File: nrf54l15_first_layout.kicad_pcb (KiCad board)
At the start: 4 copper layers, 76.4 x 51 mm, 60 parts, among them CN1 SM04B-SRSS-TB, J2 TC2030, J3 USB_C_Receptacle_PowerOnly_6P, U1 nRF54L15-QDXX, U2 nPM1300-QEXX, U3 SPV1040T, U4 S2B-PH-K-S-GW, X1 XL7EL89CKI-111YLC-32M

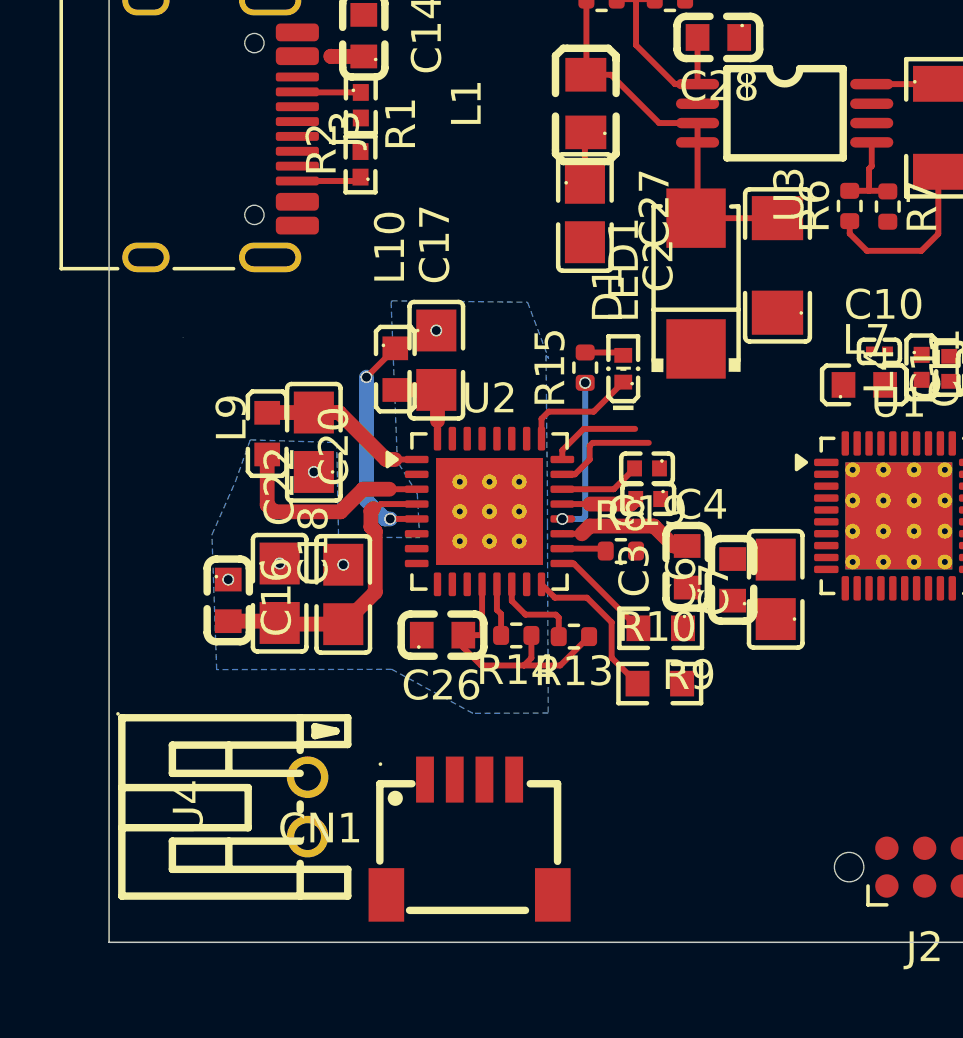
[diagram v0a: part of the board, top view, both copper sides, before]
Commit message: Update soil moisture PCB and npm1300 VDDIO routing; add espc6_ph and first layout projects.
Co-authored-by: Cursor <cursoragent@cursor.com>
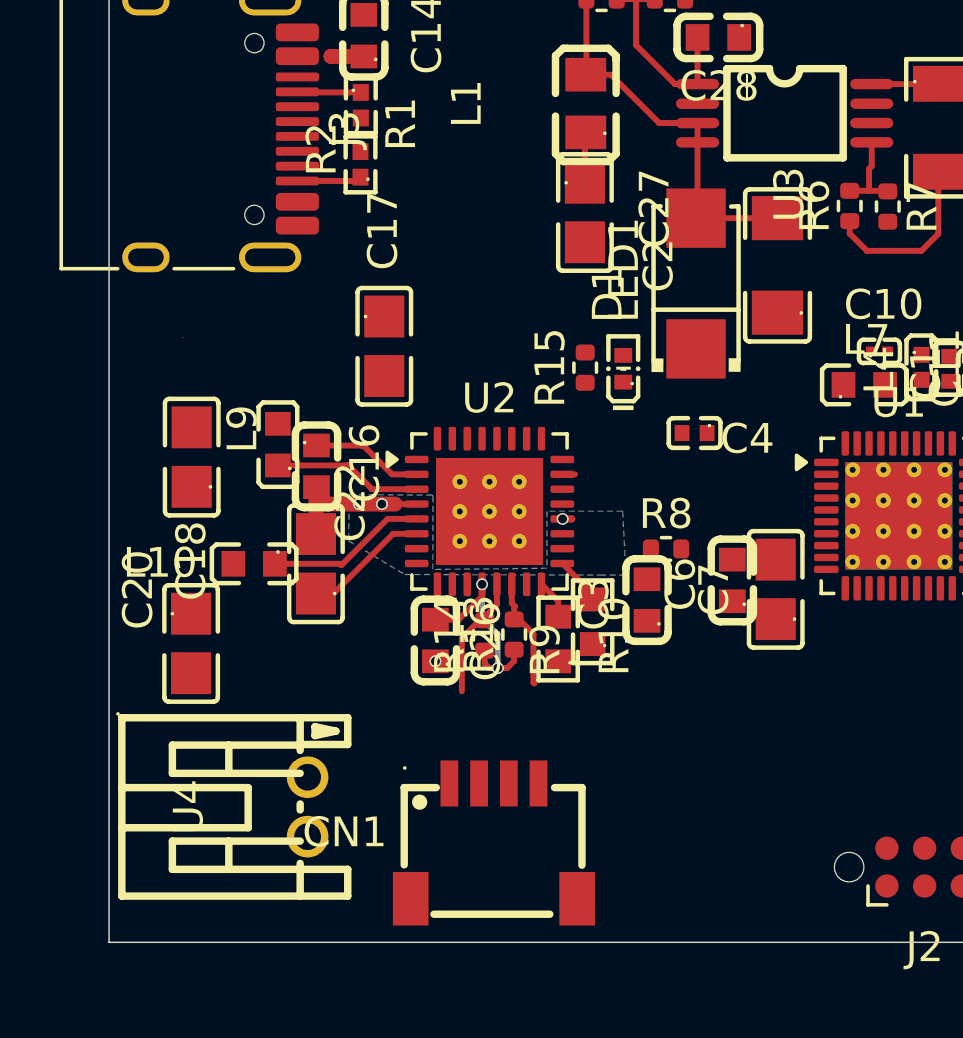
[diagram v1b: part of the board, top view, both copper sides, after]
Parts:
- removed C19: 1uF, easyeda2kicad:C0402
- moved L10 8.09 mm to (98.6, 89.3), turned to 180 degrees
- moved C16 5.40 mm to (100.7, 86.0)
- moved C20 5.38 mm to (96.5, 92.0)
- moved C18 4.14 mm to (96.5, 85.7)
- moved R10 3.73 mm to (108.8, 91.8), turned to 90 degrees
- moved C4 2.71 mm to (113.4, 84.9)
- moved R9 2.30 mm to (110.0, 91.3), turned to 90 degrees
- moved R13 2.01 mm to (107.4, 91.7), turned to 90 degrees
- moved C17 1.81 mm to (103.0, 82.0)
- moved C3 1.75 mm to (111.8, 90.5)
- moved C22 1.57 mm to (100.7, 89.3), turned to 90 degrees
- moved R8 1.52 mm to (112.5, 88.8)
- moved R14 1.06 mm to (106.4, 91.7), turned to 90 degrees
- moved CN1 0.83 mm to (106.7, 98.7)
- moved L9 0.52 mm to (99.4, 85.3)
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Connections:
- C16 pad 1: VSYS_GND -> PVSS1
- C18 pad 1: VSYS_GND -> GND
- C22 pad 1: VSYS_GND -> PVSS2
- U2 pad 2: GND -> PVSS1
- U2 pad 6: GND -> PVSS2
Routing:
- net /npm1300/VSYS: track 15.5 -> 5.33 mm, vias 2 -> 3
- net VOUT1: track 5.69 -> 0.00 mm
- net VBAT: track 4.61 -> 0.03 mm
- net PVSS2: track 0.00 -> 4.22 mm
- net Net-(U2-VSET2): track 5.31 -> 1.32 mm
- net Net-(LED1-C): track 3.93 -> 0.00 mm
- net PVSS1: track 0.00 -> 3.78 mm
- net CC1: track 5.76 -> 2.57 mm
- net VOUT2: track 3.09 -> 0.00 mm
- net CC2: track 5.24 -> 2.18 mm
- net VBUSOUT: track 2.72 -> 0.00 mm
- net VBUS: track 3.65 -> 1.11 mm
- net I2C_SDA: track 1.78 -> 4.22 mm
- net Net-(U2-SW1): track 7.14 -> 5.01 mm
- net Net-(U2-SW2): track 7.47 -> 5.43 mm, vias 2 -> 0
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- added copper zone on B.Cu, net /npm1300/VSYS
- removed copper zone on B.Cu, net VSYS_GND
